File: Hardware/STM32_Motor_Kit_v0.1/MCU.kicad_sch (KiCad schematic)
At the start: 23 parts, among them SW1 SW_DIP_x01, SW2 Push_Button_SMD_4P, SW3 Push_Button_SMD_4P, U1 STM32G431RBT6, Y1 CRYSTAL_8mHz

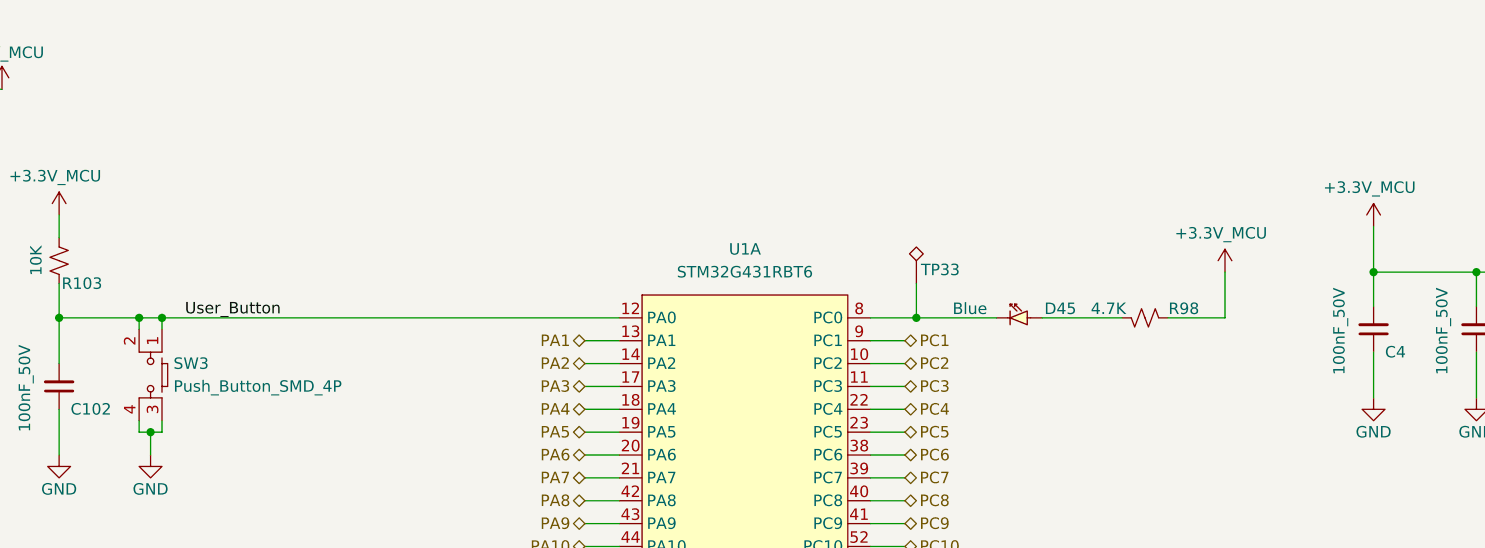
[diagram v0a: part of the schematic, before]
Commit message: Firmware Configuration added, Motor Control Pins and BackEMF Analog Pins setted.
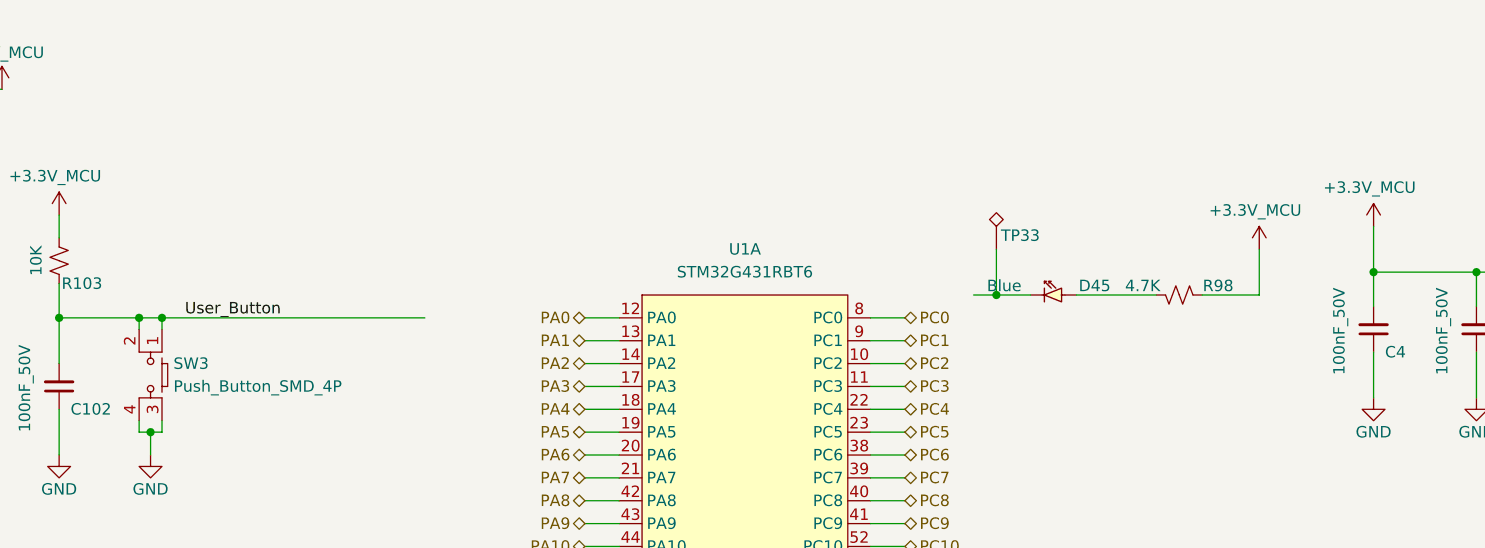
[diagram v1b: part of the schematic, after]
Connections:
- net User_Button: no longer U1.12 (PA0)
- net at D45.1, TP33.1: no longer U1.8 (PC0)
- new net PA0: U1.12 (PA0)
- new net PC0: U1.8 (PC0)
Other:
- moved on the sheet: D45, R98, TP33
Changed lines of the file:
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@@
 	)
 	(junction
-		(at 26.67 22.86)
+		(at 62.23 48.26)
 		(diameter 0)
 		(color 0 0 0 0)
 	)
 	(junction
-		(at 146.05 48.26)
+		(at 26.67 22.86)
 		(diameter 0)
 		(color 0 0 0 0)
@@
 	)
 	(junction
-		(at 62.23 48.26)
-		(diameter 0)
-		(color 0 0 0 0)
-	)
-	(junction
 		(at 59.69 48.26)
 		(diameter 0)
@@
 		(color 0 0 0 0)
 	)
+	(junction
+		(at 154.94 45.72)
+		(diameter 0)
+		(color 0 0 0 0)
+	)
 	(wire
 		(pts
@@
 	(wire
 		(pts
-			(xy 146.05 48.26) (xy 154.94 48.26)
-		)
-		(stroke
-			(width 0)
-			(type default)
-		)
-	)
-	(wire
-		(pts
 			(xy 50.8 48.26) (xy 59.69 48.26)
 		)
@@
 	(wire
 		(pts
+			(xy 109.22 48.26) (xy 113.03 48.26)
+		)
+		(stroke
+			(width 0)
+			(type default)
+		)
+	)
+	(wire
+		(pts
 			(xy 66.04 99.06) (xy 66.04 102.87)
 		)
@@
 	(wire
 		(pts
-			(xy 180.34 48.26) (xy 173.99 48.26)
+			(xy 184.15 45.72) (xy 177.8 45.72)
 		)
 		(stroke
@@
 	(wire
 		(pts
+			(xy 154.94 40.64) (xy 154.94 45.72)
+		)
+		(stroke
+			(width 0)
+			(type default)
+		)
+	)
+	(wire
+		(pts
 			(xy 194.31 109.22) (xy 203.2 109.22)
 		)
@@
 	(wire
 		(pts
-			(xy 140.97 162.56) (xy 138.43 162.56)
+			(xy 62.23 48.26) (xy 91.44 48.26)
 		)
 		(stroke
@@
 	(wire
 		(pts
-			(xy 114.3 176.53) (xy 114.3 180.34)
+			(xy 140.97 162.56) (xy 138.43 162.56)
 		)
 		(stroke
@@
 	(wire
 		(pts
-			(xy 208.28 43.18) (xy 208.28 46.99)
+			(xy 114.3 176.53) (xy 114.3 180.34)
 		)
 		(stroke
@@
 	(wire
 		(pts
-			(xy 62.23 48.26) (xy 113.03 48.26)
+			(xy 208.28 43.18) (xy 208.28 46.99)
 		)
 		(stroke
@@
 	(wire
 		(pts
-			(xy 140.97 48.26) (xy 146.05 48.26)
+			(xy 140.97 48.26) (xy 144.78 48.26)
 		)
 		(stroke
@@
 	(wire
 		(pts
-			(xy 180.34 43.18) (xy 180.34 48.26)
+			(xy 184.15 40.64) (xy 184.15 45.72)
 		)
 		(stroke
@@
 	(wire
 		(pts
-			(xy 146.05 44.45) (xy 146.05 48.26)
+			(xy 179.07 91.44) (xy 179.07 97.79)
 		)
 		(stroke
@@
 	(wire
 		(pts
-			(xy 179.07 91.44) (xy 179.07 97.79)
+			(xy 114.3 162.56) (xy 116.84 162.56)
 		)
 		(stroke
@@
 		)
 	)
-	(wire
+	(polyline
 		(pts
-			(xy 114.3 162.56) (xy 116.84 162.56)
+			(xy 85.09 86.36) (xy 55.88 86.36)
 		)
 		(stroke
@@
 		)
 	)
-	(polyline
+	(wire
 		(pts
-			(xy 85.09 86.36) (xy 55.88 86.36)
+			(xy 154.94 45.72) (xy 158.75 45.72)
 		)
 		(stroke
@@
 	(wire
 		(pts
+			(xy 152.4 45.72) (xy 154.94 45.72)
+		)
+		(stroke
+			(width 0)
+			(type default)
+		)
+	)
+	(wire
+		(pts
 			(xy 144.78 86.36) (xy 140.97 86.36)
 		)
@@
 	(wire
 		(pts
-			(xy 168.91 48.26) (xy 160.02 48.26)
+			(xy 172.72 45.72) (xy 163.83 45.72)
 		)
 		(stroke
@@
 		)
 	)
+	(hierarchical_label "PC0"
+		(shape bidirectional)
+		(at 144.78 48.26 0)
+		(fields_autoplaced yes)
+		(effects
+			(font
+				(size 1.27 1.27)
+			)
+			(justify left)
+		)
+	)
 	(hierarchical_label "PB11"
 		(shape bidirectional)
@@
 		)
 	)
+	(hierarchical_label "PA0"
+		(shape bidirectional)
+		(at 109.22 48.26 180)
+		(fields_autoplaced yes)
+		(effects
+			(font
+				(size 1.27 1.27)
+			)
+			(justify right)
+		)
+	)
 	(hierarchical_label "PA9"
 		(shape bidirectional)
@@
 	(symbol
 		(lib_id "AKE_Device:Test_Point")
-		(at 146.05 44.45 0)
+		(at 154.94 40.64 0)
 		(unit 1)
 		(exclude_from_sim no)
@@
 		(dnp no)
 		(property "Reference" "TP33"
-			(at 146.558 42.926 0)
+			(at 155.448 39.116 0)
 			(effects
 				(font
@@
 		)
 		(property "Value" "Test_Point"
-			(at 148.59 42.4179 0)
+			(at 157.48 38.6079 0)
 			(effects
 				(font
@@
 		)
 		(property "Footprint" "AKE_PCB:TEST_POINT"
-			(at 151.13 44.45 0)
+			(at 160.02 40.64 0)
 			(effects
 				(font
@@
 		)
 		(property "Datasheet" "~"
-			(at 151.13 44.45 0)
+			(at 160.02 40.64 0)
 			(effects
 				(font
@@
 		)
 		(property "Description" "test point (alternative shape)"
-			(at 146.05 44.45 0)
+			(at 154.94 40.64 0)
 			(effects
 				(font
@@
 	(symbol
 		(lib_id "AKE_Power:+3.3V")
-		(at 180.34 43.18 0)
+		(at 184.15 40.64 0)
 		(unit 1)
 		(exclude_from_sim no)
@@
 		(dnp no)
 		(property "Reference" "#PWR0153"
-			(at 180.34 46.99 0)
+			(at 184.15 44.45 0)
 			(effects
 				(font
@@
 		)
 		(property "Value" "+3.3V_MCU"
-			(at 174.752 38.862 0)
+			(at 178.562 36.322 0)
 			(effects
 				(font
@@
 		)
 		(property "Footprint" ""
-			(at 180.34 43.18 0)
+			(at 184.15 40.64 0)
 			(effects
 				(font
@@
 		)
 		(property "Datasheet" ""
-			(at 180.34 43.18 0)
+			(at 184.15 40.64 0)
 			(effects
 				(font
@@
 		)
 		(property "Description" ""
-			(at 180.34 43.18 0)
+			(at 184.15 40.64 0)
 			(effects
 				(font
@@
 	(symbol
 		(lib_id "AKE_Resistor:Resistor_US")
-		(at 171.45 48.26 90)
+		(at 175.26 45.72 90)
 		(mirror x)
 		(unit 1)
@@
 		(dnp no)
 		(property "Reference" "R98"
-			(at 175.768 47.244 90)
+			(at 179.578 44.704 90)
 			(effects
 				(font
@@
 		)
 		(property "Value" "4.7K"
-			(at 167.386 47.244 90)
+			(at 171.196 44.704 90)
 			(effects
 				(font
@@
 		)
 		(property "Footprint" "AKE_Resistor_SMD:RES_0603"
-			(at 171.45 48.26 0)
+			(at 175.26 45.72 0)
 			(effects
 				(font
@@
 		)
 		(property "Datasheet" "~"
-			(at 171.45 48.26 0)
+			(at 175.26 45.72 0)
 			(effects
 				(font
@@
 		)
 		(property "Description" ""
-			(at 171.45 48.26 0)
+			(at 175.26 45.72 0)
 			(effects
 				(font
@@
 		)
 		(property "MFG P/N" "*"
-			(at 168.91 52.07 0)
+			(at 172.72 49.53 0)
 			(effects
 				(font
@@
 	(symbol
 		(lib_id "AKE_Diode:Diode_LED")
-		(at 154.94 46.99 0)
+		(at 158.75 44.45 0)
 		(mirror x)
 		(unit 1)
@@
 		(dnp no)
 		(property "Reference" "D45"
-			(at 163.83 47.244 0)
+			(at 167.64 44.704 0)
 			(effects
 				(font
@@
 		)
 		(property "Value" "Blue"
-			(at 153.924 47.244 0)
+			(at 157.734 44.704 0)
 			(effects
 				(font
@@
 		)
 		(property "Footprint" "AKE_Led_SMD:LED_0805"
-			(at 158.115 49.53 0)
+			(at 161.925 46.99 0)
 			(effects
 				(font
@@
 		)
 		(property "Datasheet" ""
-			(at 158.115 49.53 0)
+			(at 161.925 46.99 0)
 			(effects
 				(font
@@
 		)
 		(property "Description" ""
-			(at 154.94 46.99 0)
+			(at 158.75 44.45 0)
 			(effects
 				(font
@@
 		)
 		(property "MFG P/N" "*"
-			(at 154.94 46.99 0)
+			(at 158.75 44.45 0)
 			(effects
 				(font

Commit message: 22.08.2024
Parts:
- removed C102: 100nF_50V, AKE_Capacitor_SMD:CAP_0603, symbol AKE_Capacitor:Capacitor_UnPolarised
- removed D45: Blue, AKE_Led_SMD:LED_0805, symbol AKE_Diode:Diode_LED
- removed R103: 10K, AKE_Resistor_SMD:RES_0603, symbol AKE_Resistor:Resistor_US
- removed R98: 4.7K, AKE_Resistor_SMD:RES_0603, symbol AKE_Resistor:Resistor_US
- removed SW3: Push_Button_SMD_4P, AKE_Button_SMD_TH:SW_PTS645SK50SMTR92, symbol AKE_Device:Push_Button_SMD_4P
- removed TP33: Test_Point, AKE_PCB:TEST_POINT, symbol AKE_Device:Test_Point
- C4: value 100nF_50V -> 2.2uF_10V
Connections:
- net BOOT renamed PB8
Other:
- moved on the sheet: R1, SW1

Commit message: 23.08.2024
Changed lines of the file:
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@@
 	(polyline
 		(pts
-			(xy 55.88 107.95) (xy 55.88 86.36)
+			(xy 55.88 105.41) (xy 55.88 86.36)
 		)
 		(stroke

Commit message: 12.01.2025
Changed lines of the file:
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@@
 			(effects
 				(font
-					(size 1.27 1.27)
+					(face "Arial")
+					(size 0.635 0.635)
 				)
 				(hide yes)
@@
 			(effects
 				(font
-					(size 1.27 1.27)
+					(face "Arial")
+					(size 0.635 0.635)
 				)
 				(justify right)
@@
 			(effects
 				(font
-					(size 1.27 1.27)
+					(face "Arial")
+					(size 0.635 0.635)
 				)
 				(hide yes)
@@
 			(effects
 				(font
-					(size 1.27 1.27)
+					(face "Arial")
+					(size 0.635 0.635)
 				)
 				(hide yes)
@@
 			(effects
 				(font
-					(size 1.27 1.27)
+					(face "Arial")
+					(size 0.635 0.635)
 				)
 				(hide yes)
@@
 			(effects
 				(font
-					(size 1.27 1.27)
+					(face "Arial")
+					(size 0.635 0.635)
 				)
 			)
@@
 			(effects
 				(font
-					(size 1.27 1.27)
+					(face "Arial")
+					(size 0.635 0.635)
 				)
 				(justify right)
@@
 			(effects
 				(font
-					(size 1.27 1.27)
+					(face "Arial")
+					(size 0.635 0.635)
 				)
 				(hide yes)
@@
 			(effects
 				(font
-					(size 1.27 1.27)
+					(face "Arial")
+					(size 0.635 0.635)
 				)
 				(hide yes)
@@
 			(effects
 				(font
-					(size 1.27 1.27)
+					(face "Arial")
+					(size 0.635 0.635)
 				)
 				(hide yes)
@@
 			(effects
 				(font
-					(size 1.27 1.27)
+					(face "Arial")
+					(size 0.635 0.635)
 				)
 				(justify right)
@@
 			(effects
 				(font
-					(size 1.27 1.27)
+					(face "Arial")
+					(size 0.635 0.635)
 				)
 				(justify right)
@@
 			(effects
 				(font
-					(size 1.27 1.27)
+					(face "Arial")
+					(size 0.635 0.635)
 				)
 			)
@@
 			(effects
 				(font
-					(size 1.27 1.27)
+					(face "Arial")
+					(size 0.635 0.635)
 				)
 				(hide yes)
@@
 			(effects
 				(font
-					(size 1.27 1.27)
+					(face "Arial")
+					(size 0.635 0.635)
 				)
 				(hide yes)
@@
 			(effects
 				(font
-					(size 1.27 1.27)
+					(face "Arial")
+					(size 0.635 0.635)
 				)
 			)
@@
 			(effects
 				(font
-					(size 1.27 1.27)
+					(face "Arial")
+					(size 0.635 0.635)
 				)
 			)
@@
 			(effects
 				(font
-					(size 1.27 1.27)
+					(face "Arial")
+					(size 0.635 0.635)
 				)
 			)
@@
 			(effects
 				(font
-					(size 1.27 1.27)
+					(face "Arial")
+					(size 0.635 0.635)
 				)
 				(hide yes)
@@
 			(effects
 				(font
-					(size 1.27 1.27)
+					(face "Arial")
+					(size 0.635 0.635)
 				)
 				(hide yes)
@@
 			(effects
 				(font
-					(size 1.27 1.27)
+					(face "Arial")
+					(size 0.635 0.635)
 				)
 			)
@@
 			(effects
 				(font
-					(size 1.27 1.27)
+					(face "Arial")
+					(size 0.635 0.635)
 				)
 				(justify right)
@@
 			(effects
 				(font
-					(size 1.27 1.27)
+					(face "Arial")
+					(size 0.635 0.635)
 				)
 				(justify right)
@@
 			(effects
 				(font
-					(size 1.27 1.27)
+					(face "Arial")
+					(size 0.635 0.635)
 				)
 				(hide yes)
@@
 			(effects
 				(font
-					(size 1.27 1.27)
+					(face "Arial")
+					(size 0.635 0.635)
 				)
 				(hide yes)
@@
 			(effects
 				(font
-					(size 1.27 1.27)
+					(face "Arial")
+					(size 0.635 0.635)
 				)
 				(justify right)
@@
 			(effects
 				(font
-					(size 1.27 1.27)
+					(face "Arial")
+					(size 0.635 0.635)
 				)
 			)
@@
 			(effects
 				(font
-					(size 1.27 1.27)
+					(face "Arial")
+					(size 0.635 0.635)
 				)
 			)
@@
 			(effects
 				(font
-					(size 1.27 1.27)
+					(face "Arial")
+					(size 0.635 0.635)
 				)
 				(hide yes)
@@
 			(effects
 				(font
-					(size 1.27 1.27)
+					(face "Arial")
+					(size 0.635 0.635)
 				)
 				(justify right)
@@
 			(effects
 				(font
-					(size 1.27 1.27)
+					(face "Arial")
+					(size 0.635 0.635)
 				)
 				(justify right)
@@
 			(effects
 				(font
-					(size 1.27 1.27)
+					(face "Arial")
+					(size 0.635 0.635)
 				)
 				(hide yes)
@@
 			(effects
 				(font
-					(size 1.27 1.27)
+					(face "Arial")
+					(size 0.635 0.635)
 				)
 				(hide yes)
@@
 			(effects
 				(font
-					(size 1.27 1.27)
+					(face "Arial")
+					(size 0.635 0.635)
 				)
 				(hide yes)
@@
 			(effects
 				(font
-					(size 1.27 1.27)
+					(face "Arial")
+					(size 0.635 0.635)
 				)
 				(justify left)
@@
 			(effects
 				(font
-					(size 1.27 1.27)
-				)
-				(hide yes)
+					(face "Arial")
+					(size 0.635 0.635)
+				)
+				(hide yes)
